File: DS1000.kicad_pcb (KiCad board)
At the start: 2 copper layers, 9.8 x 18.4 mm, 2 parts

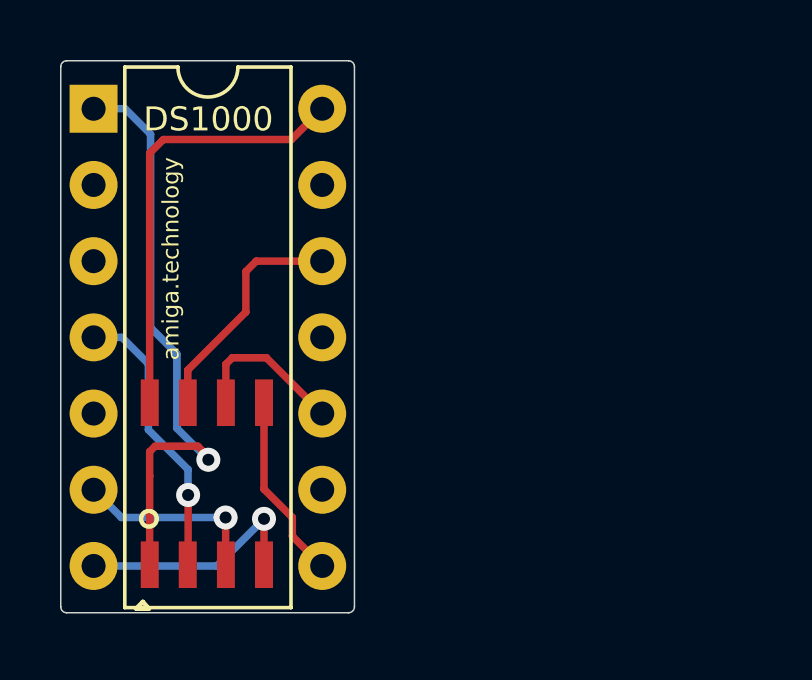
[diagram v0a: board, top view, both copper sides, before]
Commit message: Update to Revision B
- move all traces to the bottom side for a cleaner look
- actually add some schematics (and symbols and footprints)
- remove cache files

This was redone with Kicad 6.0rc (nightly build)
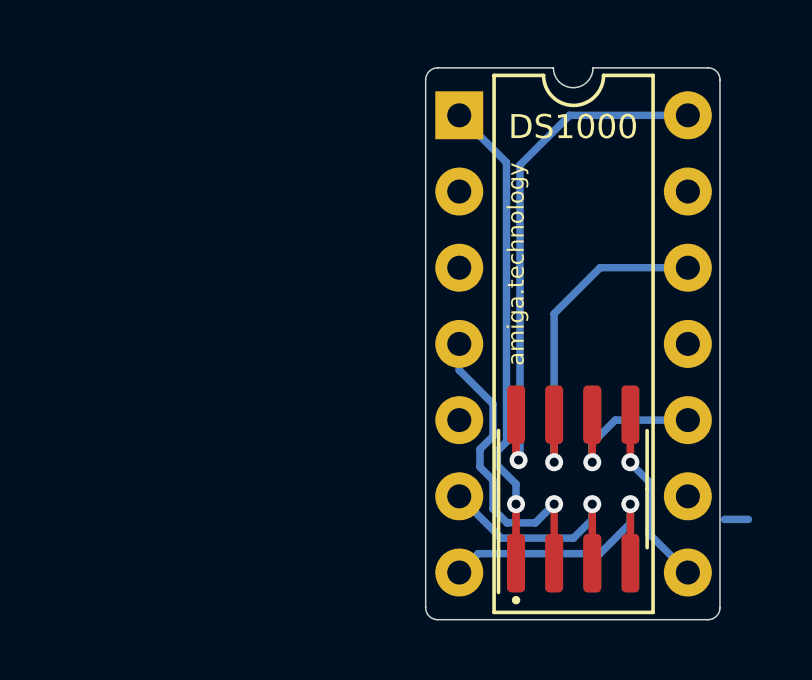
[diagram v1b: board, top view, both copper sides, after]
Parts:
- removed  : , 4ms/4ms-kicad-lib/lib-footprints/4ms_Package_SOIC.pretty:SOIC-8_3.9x4.9mm_Pitch1.27mm
- added U1: DS1000-25_(SOIC), DS1000:SOIC-8_3.9x4.9mm_P1.27mm, F.Cu at (127.8, 55.4)
- DS1000: footprint 4ms/4ms-kicad-lib/lib-footprints/4ms_Package_DIP.pretty:DIP-14_W7.62mm -> Package_DIP:DIP-14_W7.62mm
- moved DS1000 12.2 mm to (124.0, 42.9)
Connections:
- DS1000 pad 1: (no net) -> Net-(U1-Pad1)
- DS1000 pad 10: (no net) -> Net-(U1-Pad6)
- DS1000 pad 11: (no net) -> unconnected-(U2-Pad11)
- DS1000 pad 12: (no net) -> Net-(U1-Pad7)
- DS1000 pad 13: (no net) -> unconnected-(U2-Pad13)
- DS1000 pad 14: (no net) -> Net-(U1-Pad8)
- DS1000 pad 2: (no net) -> unconnected-(U2-Pad2)
- DS1000 pad 3: (no net) -> unconnected-(U2-Pad3)
- DS1000 pad 4: (no net) -> Net-(U1-Pad2)
- DS1000 pad 6: (no net) -> Net-(U1-Pad3)
- DS1000 pad 7: (no net) -> Net-(U1-Pad4)
- DS1000 pad 8: (no net) -> Net-(U1-Pad5)
- DS1000 pad 9: (no net) -> unconnected-(U2-Pad9)
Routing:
- net (no net): track 77.8 -> 0.80 mm, vias 4 -> 0
- net Net-(U1-Pad8): track 0.00 -> 18.3 mm, vias 0 -> 1
- net Net-(U1-Pad1): track 0.00 -> 16.0 mm, vias 0 -> 1
- net Net-(U1-Pad7): track 0.00 -> 12.0 mm, vias 0 -> 1
- net Net-(U1-Pad2): track 0.00 -> 10.7 mm, vias 0 -> 1
- net Net-(U1-Pad4): track 0.00 -> 8.73 mm, vias 0 -> 1
- net Net-(U1-Pad3): track 0.00 -> 6.52 mm, vias 0 -> 1
- net Net-(U1-Pad5): track 0.00 -> 6.16 mm, vias 0 -> 1
- net Net-(U1-Pad6): track 0.00 -> 5.73 mm, vias 0 -> 1
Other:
- outline, holes or cut-outs redrawn
- net class Default removed
- board text added: "revision B"
